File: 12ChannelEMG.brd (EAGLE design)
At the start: 65.9 x 15.4 mm, 24 parts

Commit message: Duplicated first channel to make second channel
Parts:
- added C10: 3.3uF, resistor:C1206K
- added C11, C12: 0.22uF, rcl:C0603K
- added C13, C14, C8, C9: 0.1uF, resistor:C1206K
- added D2: BAT54, diode:SOT23
- added R11: 50k, rcl:R0805
- added R12, R20: 100, resistor:R0603
- added R13: 10k, rcl:R0603
- added R14: 200, rcl:R0603
- added R15, R16: 82k, resistor:R0603
- added R17: 300, resistor:R0603
- added R18: 100k, resistor:R0603
- added R19: 56k, resistor:R0603
- added U$4: INA101KU, 12-ChannelEMG:SOIC167.5MM
- added U$5: LMC6492, 12-ChannelEMG:SOIC14
- added U$6: PV36504, 12-ChannelEMG:PV36W
- added VIN+1, VIN-1: 1.5MMJACK, 12-ChannelEMG:1.5MMTOUCHPROOFJACK
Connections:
- new net N$13: R11.2, U$4.12, U$4.13
- new net N$20: U$4.3, VIN-1.1
- new net N$21: R12.2, U$5.2, U$6.1
- new net N$22: R12.1, U$4.1
- new net N$23: C10.1, U$5.1, U$6.2
- new net N$24: C10.2, R13.2, U$5.5
- new net N$25: R14.1, U$5.6, U$5.7
- new net N$26: R14.2, R20.1, U$5.9
- new net N$27: D2.1, U$5.8
- new net N$28: C13.1, R16.1, U$5.12
- new net N$29: D2.3, R15.1, R17.1, R20.2
- new net N$30: C14.2, R19.2, U$5.14
- new net N$31: R18.1, R19.1, U$5.13
- new net N$32: C14.1, R15.2, R16.2
- new net N$33: R11.1, U$4.4, U$4.5
- new net N$34: U$4.14, VIN+1.1
- net GND: now also C11.2, C12.2, C13.2, C8.2, C9.2, R13.1, R17.2, R18.2, U$5.10, U$5.3
- net VCC+: now also C11.1, C8.1, U$4.2, U$5.4
- net VCC-: now also C12.1, C9.1, U$4.15, U$5.11
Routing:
- net VCC-: track 36.8 -> 86.4 mm
- net VCC+: track 28.1 -> 71.1 mm, vias 2 -> 5
- net N$21: track 0.00 -> 18.0 mm, vias 0 -> 1
- net N$34: track 0.00 -> 15.1 mm, vias 0 -> 1
- net N$29: track 0.00 -> 13.4 mm, vias 0 -> 1
- net N$23: track 0.00 -> 10.1 mm
- net N$24: track 0.00 -> 9.66 mm
- net N$32: track 0.00 -> 8.14 mm
- net N$26: track 0.00 -> 7.74 mm
- net N$20: track 0.00 -> 7.35 mm
- net N$30: track 0.00 -> 5.88 mm, vias 0 -> 1
- net N$28: track 0.00 -> 5.28 mm, vias 0 -> 1
- net N$13: track 0.00 -> 4.66 mm, vias 0 -> 1
- net N$33: track 0.00 -> 4.66 mm, vias 0 -> 1
- net N$31: track 0.00 -> 4.54 mm
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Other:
- board size 65.9 x 15.4 mm -> 65.9 x 269.4 mm

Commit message: Three Channels
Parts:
- added C15, C16, C20, C21: 0.1uF, resistor:C1206K
- added C17: 3.3uF, resistor:C1206K
- added C18, C19: 0.22uF, rcl:C0603K
- added D3: BAT54, diode:SOT23
- added R21: 50k, rcl:R0805
- added R22, R30: 100, resistor:R0603
- added R23: 10k, rcl:R0603
- added R24: 200, rcl:R0603
- added R25, R26: 82k, resistor:R0603
- added R27: 300, resistor:R0603
- added R28: 100k, resistor:R0603
- added R29: 56k, resistor:R0603
- added U$7: INA101KU, 12-ChannelEMG:SOIC167.5MM
- added U$8: LMC6492, 12-ChannelEMG:SOIC14
- added U$9: PV36504, 12-ChannelEMG:PV36W
- added VIN+2, VIN-2: 1.5MMJACK, 12-ChannelEMG:1.5MMTOUCHPROOFJACK
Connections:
- new net N$35: R21.2, U$7.12, U$7.13
- new net N$36: U$7.3, VIN-2.1
- new net N$37: R22.2, U$8.2, U$9.1
- new net N$38: R22.1, U$7.1
- new net N$39: C17.1, U$8.1, U$9.2
- new net N$40: C17.2, R23.2, U$8.5
- new net N$41: R24.1, U$8.6, U$8.7
- new net N$42: R24.2, R30.1, U$8.9
- new net N$43: D3.1, U$8.8
- new net N$44: C20.1, R26.1, U$8.12
- new net N$45: D3.3, R25.1, R27.1, R30.2
- new net N$46: C21.2, R29.2, U$8.14
- new net N$47: R28.1, R29.1, U$8.13
- new net N$48: C21.1, R25.2, R26.2
- new net N$49: R21.1, U$7.4, U$7.5
- new net N$50: U$7.14, VIN+2.1
- net GND: now also C15.2, C16.2, C18.2, C19.2, C20.2, R23.1, R27.2, R28.2, U$8.10, U$8.3
- net VCC+: now also C15.1, C18.1, U$7.2, U$8.4
- net VCC-: now also C16.1, C19.1, U$7.15, U$8.11
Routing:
- net VCC-: track 86.4 -> 136.4 mm
- net VCC+: track 71.1 -> 114.1 mm, vias 5 -> 8
- net N$37: track 0.00 -> 18.0 mm, vias 0 -> 1
- net N$50: track 0.00 -> 15.1 mm, vias 0 -> 1
- net N$45: track 0.00 -> 13.4 mm, vias 0 -> 1
- net N$39: track 0.00 -> 10.1 mm
- net N$40: track 0.00 -> 9.66 mm
- net N$48: track 0.00 -> 8.14 mm
- net N$42: track 0.00 -> 7.74 mm
- net N$36: track 0.00 -> 7.35 mm
- net N$46: track 0.00 -> 5.88 mm, vias 0 -> 1
- net N$44: track 0.00 -> 5.28 mm, vias 0 -> 1
- net N$35: track 0.00 -> 4.66 mm, vias 0 -> 1
- net N$49: track 0.00 -> 4.66 mm, vias 0 -> 1
- net N$47: track 0.00 -> 4.54 mm
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
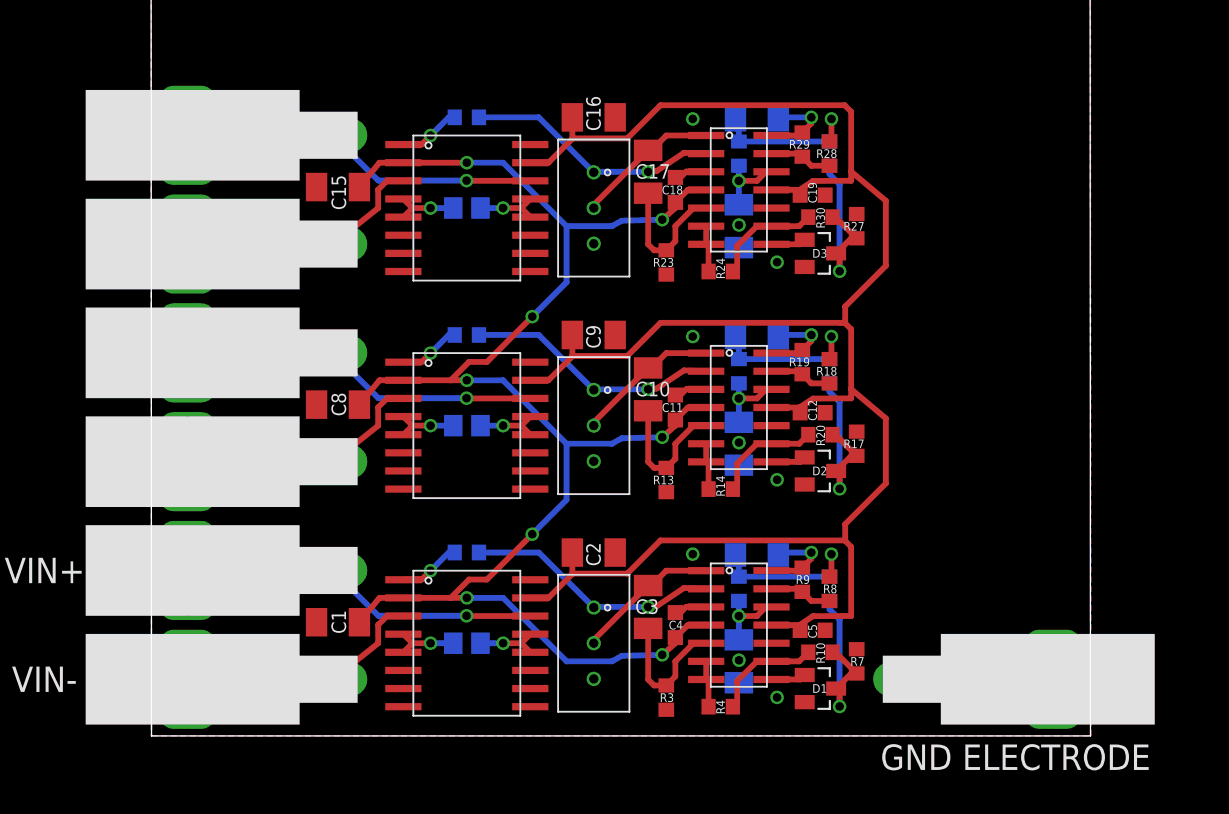
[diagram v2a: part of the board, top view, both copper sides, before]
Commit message: Removed old connectors
Added ground jumper for ground electrode
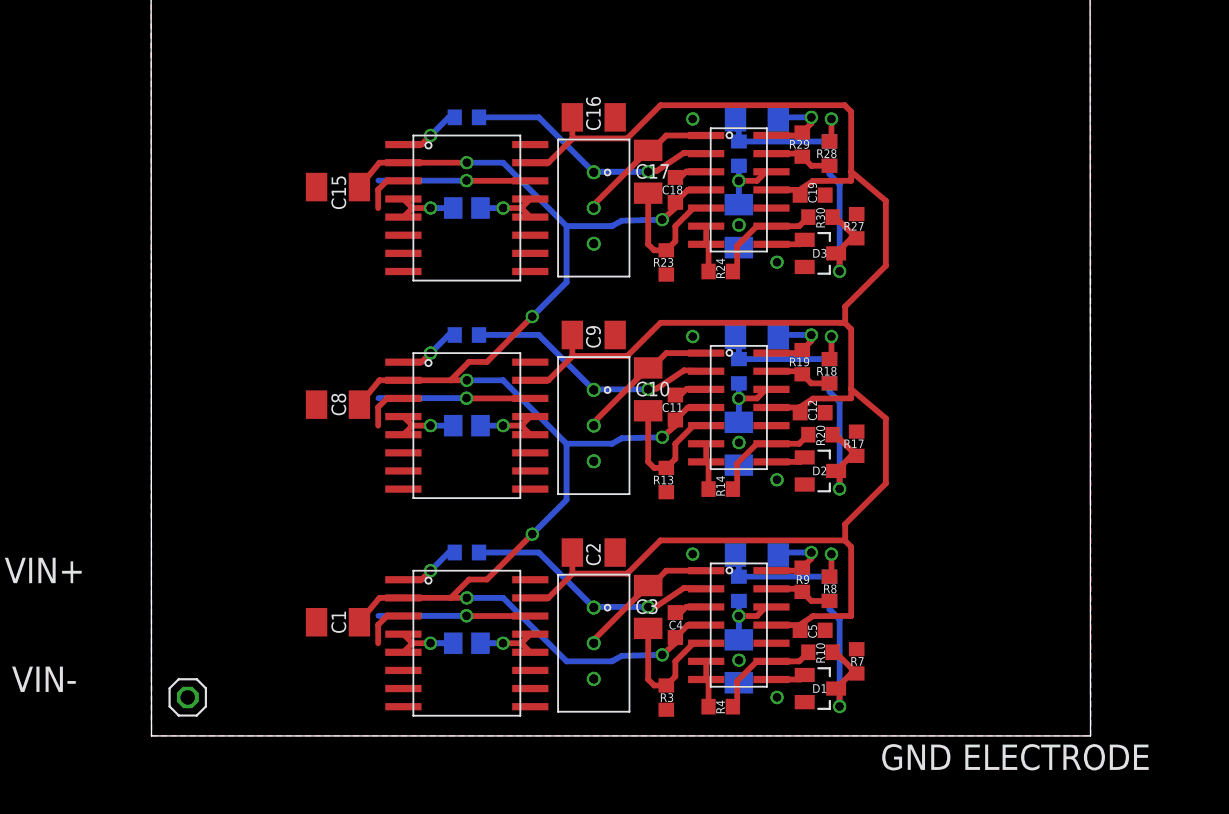
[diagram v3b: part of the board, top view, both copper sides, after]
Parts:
- removed VIN+, VIN+1, VIN+2, VIN-, VIN-1, VIN-2: 1.5MMJACK, 12-ChannelEMG:1.5MMTOUCHPROOFJACK
- GND: value 1.5MMJACK -> GND; device 12-ChannelEMG:1.5MMTOUCHPROOFJACK -> pinhead:1X01
- moved GND 55.5 mm to (2.54, 2.54), turned to 0 degrees
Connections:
- net N$20: no longer VIN-1.1
- net N$34: no longer VIN+1.1
- net N$36: no longer VIN-2.1
- net N$50: no longer VIN+2.1
- net N$6: no longer VIN-.1
- net N$7: no longer VIN+.1
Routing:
- net N$7: track 15.1 -> 10.6 mm
- net N$34: track 15.1 -> 10.6 mm
- net N$50: track 15.1 -> 10.6 mm
- net N$36: track 7.35 -> 3.31 mm
- net N$20: track 7.35 -> 3.31 mm
- net N$6: track 7.35 -> 3.31 mm
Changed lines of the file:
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@@
 <setting verticaltext="up"/>
 </settings>
-<grid distance="50" unitdist="mil" unit="mil" style="lines" multiple="1" display="yes" altdistance="5" altunitdist="mil" altunit="mil"/>
+<grid distance="5" unitdist="mil" unit="mil" style="lines" multiple="1" display="yes" altdistance="5" altunitdist="mil" altunit="mil"/>
 <layers>
 <layer number="1" name="Top" color="4" fill="1" visible="yes" active="yes"/>
@@
 <attribute name="NAME" x="47.168915625" y="4.90091875" size="0.6096" layer="25" rot="R90"/>
 </element>
-<element name="VIN+" library="12-ChannelEMG" package="1.5MMTOUCHPROOFJACK" value="1.5MMJACK" x="7.62" y="11.43"/>
-<element name="VIN-" library="12-ChannelEMG" package="1.5MMTOUCHPROOFJACK" value="1.5MMJACK" x="7.62" y="3.81"/>
-<element name="GND" library="12-ChannelEMG" package="1.5MMTOUCHPROOFJACK" value="1.5MMJACK" x="58.039" y="3.81" rot="R180"/>
 <element name="U$4" library="12-ChannelEMG" package="SOIC167.5MM" value="INA101KU" x="22.0871375" y="21.574346875"/>
 <element name="R11" library="rcl" package="R0805" value="50k" x="22.0871375" y="21.574346875" smashed="yes" rot="MR180">
@@
 <attribute name="NAME" x="47.168915625" y="20.14091875" size="0.6096" layer="25" rot="R90"/>
 </element>
-<element name="VIN+1" library="12-ChannelEMG" package="1.5MMTOUCHPROOFJACK" value="1.5MMJACK" x="7.62" y="26.67"/>
-<element name="VIN-1" library="12-ChannelEMG" package="1.5MMTOUCHPROOFJACK" value="1.5MMJACK" x="7.62" y="19.05"/>
 <element name="U$7" library="12-ChannelEMG" package="SOIC167.5MM" value="INA101KU" x="22.0871375" y="36.814346875"/>
 <element name="R21" library="rcl" package="R0805" value="50k" x="22.0871375" y="36.814346875" smashed="yes" rot="MR180">
@@
 <attribute name="NAME" x="47.168915625" y="35.38091875" size="0.6096" layer="25" rot="R90"/>
 </element>
-<element name="VIN+2" library="12-ChannelEMG" package="1.5MMTOUCHPROOFJACK" value="1.5MMJACK" x="7.62" y="41.91"/>
-<element name="VIN-2" library="12-ChannelEMG" package="1.5MMTOUCHPROOFJACK" value="1.5MMJACK" x="7.62" y="34.29"/>
+<element name="GND" library="pinhead" package="1X01" value="GND" x="2.54" y="2.54" smashed="yes">
+<attribute name="VALUE" x="4.064" y="1.143" size="1.27" layer="27"/>
+</element>
 </elements>
 <signals>
@@
 <wire x1="37.465" y1="8.89" x2="38.835484375" y2="8.89" width="0.4064" layer="1"/>
 <wire x1="38.835484375" y1="8.89" x2="38.8511375" y2="8.874346875" width="0.4064" layer="1"/>
-<contactref element="GND" pad="1"/>
 <contactref element="C9" pad="2"/>
 <contactref element="C8" pad="2"/>
@@
 <wire x1="37.465" y1="39.37" x2="38.835484375" y2="39.37" width="0.4064" layer="1"/>
 <wire x1="38.835484375" y1="39.37" x2="38.8511375" y2="39.354346875" width="0.4064" layer="1"/>
+<contactref element="GND" pad="1"/>
 </signal>
 <signal name="N$6">
 <contactref element="U$1" pad="3"/>
-<contactref element="VIN-" pad="1"/>
 <wire x1="17.6421375" y1="8.239346875" x2="16.494346875" y2="8.239346875" width="0.4064" layer="1"/>
 <wire x1="16.494346875" y1="8.239346875" x2="15.875" y2="7.62" width="0.4064" layer="1"/>
 <wire x1="15.875" y1="7.62" x2="15.875" y2="6.33" width="0.4064" layer="1"/>
-<wire x1="15.875" y1="6.33" x2="12.72" y2="3.81" width="0.4064" layer="1"/>
 </signal>
 <signal name="N$5">
@@
 <signal name="N$7">
 <contactref element="U$1" pad="14"/>
-<contactref element="VIN+" pad="1"/>
 <wire x1="26.5321375" y1="8.239346875" x2="22.240653125" y2="8.239346875" width="0.4064" layer="1"/>
 <wire x1="22.240653125" y1="8.239346875" x2="22.06625" y2="8.255" width="0.4064" layer="1"/>
 <via x="22.06625" y="8.255" extent="1-16" drill="0.6"/>
 <wire x1="22.06625" y1="8.255" x2="15.895" y2="8.255" width="0.4064" layer="16"/>
-<wire x1="15.895" y1="8.255" x2="12.72" y2="11.43" width="0.4064" layer="16"/>
 </signal>
 <signal name="N$13">
@@
 <signal name="N$20">
 <contactref element="U$4" pad="3"/>
-<contactref element="VIN-1" pad="1"/>
 <wire x1="17.6421375" y1="23.479346875" x2="16.494346875" y2="23.479346875" width="0.4064" layer="1"/>
 <wire x1="16.494346875" y1="23.479346875" x2="15.875" y2="22.86" width="0.4064" layer="1"/>
 <wire x1="15.875" y1="22.86" x2="15.875" y2="21.57" width="0.4064" layer="1"/>
-<wire x1="15.875" y1="21.57" x2="12.72" y2="19.05" width="0.4064" layer="1"/>
 </signal>
 <signal name="N$21">
@@
 <signal name="N$34">
 <contactref element="U$4" pad="14"/>
-<contactref element="VIN+1" pad="1"/>
 <wire x1="26.5321375" y1="23.479346875" x2="22.240653125" y2="23.479346875" width="0.4064" layer="1"/>
 <wire x1="22.240653125" y1="23.479346875" x2="22.06625" y2="23.495" width="0.4064" layer="1"/>
 <via x="22.06625" y="23.495" extent="1-16" drill="0.6"/>
 <wire x1="22.06625" y1="23.495" x2="15.895" y2="23.495" width="0.4064" layer="16"/>
-<wire x1="15.895" y1="23.495" x2="12.72" y2="26.67" width="0.4064" layer="16"/>
 </signal>
 <signal name="N$35">
@@
 <signal name="N$36">
 <contactref element="U$7" pad="3"/>
-<contactref element="VIN-2" pad="1"/>
 <wire x1="17.6421375" y1="38.719346875" x2="16.494346875" y2="38.719346875" width="0.4064" layer="1"/>
 <wire x1="16.494346875" y1="38.719346875" x2="15.875" y2="38.1" width="0.4064" layer="1"/>
 <wire x1="15.875" y1="38.1" x2="15.875" y2="36.81" width="0.4064" layer="1"/>
-<wire x1="15.875" y1="36.81" x2="12.72" y2="34.29" width="0.4064" layer="1"/>
 </signal>
 <signal name="N$37">
@@
 <signal name="N$50">
 <contactref element="U$7" pad="14"/>
-<contactref element="VIN+2" pad="1"/>
 <wire x1="26.5321375" y1="38.719346875" x2="22.240653125" y2="38.719346875" width="0.4064" layer="1"/>
 <wire x1="22.240653125" y1="38.719346875" x2="22.06625" y2="38.735" width="0.4064" layer="1"/>
 <via x="22.06625" y="38.735" extent="1-16" drill="0.6"/>
 <wire x1="22.06625" y1="38.735" x2="15.895" y2="38.735" width="0.4064" layer="16"/>
-<wire x1="15.895" y1="38.735" x2="12.72" y2="41.91" width="0.4064" layer="16"/>
 </signal>
 </signals>
-<errors>
-</errors>
 </board>
 </drawing>

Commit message: Two channels, problems fixed
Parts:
- removed C15, C16, C20, C21: 0.1uF, resistor:C1206K
- removed C17: 3.3uF, resistor:C1206K
- removed C18, C19: 0.22uF, rcl:C0603K
- removed D3: BAT54, diode:SOT23
- removed R21: 50k, rcl:R0805
- removed R22, R30: 100, resistor:R0603
- removed R23: 10k, rcl:R0603
- removed R24: 200, rcl:R0603
- removed R25, R26: 82k, resistor:R0603
- removed R27: 300, resistor:R0603
- removed R28: 100k, resistor:R0603
- removed R29: 56k, resistor:R0603
- removed U$8: LMC6492, 12-ChannelEMG:SOIC14
- removed U$9: PV36504, 12-ChannelEMG:PV36W
- added U$10: 2PIN, 12-ChannelEMG:2PIN
- U$7: value INA101KU -> 2PIN; device 12-ChannelEMG:SOIC167.5MM -> 12-ChannelEMG:2PIN
- moved U$7 23.0 mm to (4.93, 21.5)
- moved R13 5.83 mm to (30.3, 16.7)
- moved C10 5.83 mm to (29.0, 23.1)
- moved C11 5.83 mm to (31.0, 21.8)
- moved C12 5.83 mm to (40.6, 21.5)
- moved C13 5.83 mm to (35.4, 19.3)
- moved C9 5.83 mm to (25.2, 26.9)
- moved D2 5.83 mm to (41.1, 17.4)
- moved R11 5.83 mm to (16.3, 20.6)
- moved R12 5.83 mm to (16.3, 26.9)
- moved R14 5.83 mm to (34.1, 16.1)
- moved R15 5.83 mm to (41.7, 24.4)
- moved R16 5.83 mm to (35.4, 24.4)
- moved R18 5.83 mm to (41.7, 24.4)
- moved R19 5.83 mm to (39.8, 25.0)
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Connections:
- removed net N$35: R21.2, U$7.12, U$7.13
- removed net N$36: U$7.3
- removed net N$37: R22.2, U$8.2, U$9.1
- removed net N$38: R22.1, U$7.1
- removed net N$39: C17.1, U$8.1, U$9.2
- removed net N$40: C17.2, R23.2, U$8.5
- removed net N$41: R24.1, U$8.6, U$8.7
- removed net N$42: R24.2, R30.1, U$8.9
- removed net N$43: D3.1, U$8.8
- removed net N$44: C20.1, R26.1, U$8.12
- removed net N$45: D3.3, R25.1, R27.1, R30.2
- removed net N$46: C21.2, R29.2, U$8.14
- removed net N$47: R28.1, R29.1, U$8.13
- removed net N$48: C21.1, R25.2, R26.2
- removed net N$49: R21.1, U$7.4, U$7.5
- removed net N$50: U$7.14
- net GND: no longer C15.2, C16.2, C18.2, C19.2, C20.2, R23.1, R27.2, R28.2, U$8.10, U$8.3
- net N$20: now also U$7.2
- net N$34: now also U$7.1
- net N$6: now also U$10.2
- net N$7: now also U$10.1
- net VCC+: no longer C15.1, C18.1, U$7.2, U$8.4
- net VCC-: no longer C16.1, C19.1, U$7.15, U$8.11
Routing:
- net VCC-: track 136.4 -> 86.7 mm
- net VCC+: track 114.1 -> 74.1 mm, vias 8 -> 5
- net N$37: track 18.0 -> 0.00 mm, vias 1 -> 0
- net N$45: track 13.4 -> 0.00 mm, vias 1 -> 0
- net N$50: track 10.6 -> 0.00 mm, vias 1 -> 0
- net N$39: track 10.1 -> 0.00 mm
- net N$40: track 9.66 -> 0.00 mm
- net N$48: track 8.14 -> 0.00 mm
- net N$42: track 7.74 -> 0.00 mm
- net N$46: track 5.88 -> 0.00 mm, vias 1 -> 0
- net N$44: track 5.28 -> 0.00 mm, vias 1 -> 0
- net N$7: track 10.6 -> 15.9 mm
- net N$34: track 10.6 -> 15.9 mm
- net N$20: track 3.31 -> 8.31 mm
- net N$6: track 3.31 -> 8.31 mm
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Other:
- board size 65.9 x 269.4 mm -> 47.4 x 269.2 mm
- board text removed: "GND ELECTRODE"
- board text removed: "VIN+"
- board text removed: "VIN-"

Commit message: Channel 4
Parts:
- added C15, C16, C20, C21, C22, C23, C27, C28: 0.1uF, resistor:C1206K
- added C17, C24: 3.3uF, resistor:C1206K
- added C18, C19, C25, C26: 0.22uF, rcl:C0603K
- added D3, D4: BAT54, diode:SOT23
- added R21, R31: 50k, rcl:R0805
- added R22, R30, R32, R40: 100, resistor:R0603
- added R23, R33: 10k, rcl:R0603
- added R24, R34: 200, rcl:R0603
- added R25, R26, R35, R36: 82k, resistor:R0603
- added R27, R37: 300, resistor:R0603
- added R28, R38: 100k, resistor:R0603
- added R29, R39: 56k, resistor:R0603
- added U$11, U$15: PV36504, 12-ChannelEMG:PV36W
- added U$12, U$16: 2PIN, 12-ChannelEMG:2PIN
- added U$13, U$8: INA101KU, 12-ChannelEMG:SOIC167.5MM
- added U$14, U$9: LMC6492, 12-ChannelEMG:SOIC14
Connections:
- new net N$35: R21.2, U$8.12, U$8.13
- new net N$36: U$12.2, U$8.3
- new net N$37: R22.2, U$11.1, U$9.2
- new net N$38: R22.1, U$8.1
- new net N$39: C17.1, U$11.2, U$9.1
- new net N$40: C17.2, R23.2, U$9.5
- new net N$41: R24.1, U$9.6, U$9.7
- new net N$42: R24.2, R30.1, U$9.9
- new net N$43: D3.1, U$9.8
- new net N$44: C20.1, R26.1, U$9.12
- new net N$45: D3.3, R25.1, R27.1, R30.2
- new net N$46: C21.2, R29.2, U$9.14
- new net N$47: R28.1, R29.1, U$9.13
- new net N$48: C21.1, R25.2, R26.2
- new net N$49: R21.1, U$8.4, U$8.5
- new net N$50: U$12.1, U$8.14
- new net N$51: R31.2, U$13.12, U$13.13
- new net N$52: U$13.3, U$16.2
- new net N$53: R32.2, U$14.2, U$15.1
- new net N$54: R32.1, U$13.1
- new net N$55: C24.1, U$14.1, U$15.2
- new net N$56: C24.2, R33.2, U$14.5
- new net N$57: R34.1, U$14.6, U$14.7
- new net N$58: R34.2, R40.1, U$14.9
- new net N$59: D4.1, U$14.8
- new net N$60: C27.1, R36.1, U$14.12
- new net N$61: D4.3, R35.1, R37.1, R40.2
- new net N$62: C28.2, R39.2, U$14.14
- new net N$63: R38.1, R39.1, U$14.13
- new net N$64: C28.1, R35.2, R36.2
- new net N$65: R31.1, U$13.4, U$13.5
- new net N$66: U$13.14, U$16.1
- net GND: now also C15.2, C16.2, C18.2, C19.2, C20.2, C22.2, C23.2, C25.2, C26.2, C27.2, R23.1, R27.2, R28.2, R33.1, R37.2, R38.2, U$14.10, U$14.3, U$9.10, U$9.3
- net VCC+: now also C15.1, C18.1, C22.1, C25.1, U$13.2, U$14.4, U$8.2, U$9.4
- net VCC-: now also C16.1, C19.1, C23.1, C26.1, U$13.15, U$14.11, U$8.15, U$9.11
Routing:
- net VCC-: track 86.7 -> 182.7 mm
- net VCC+: track 74.1 -> 158.7 mm, vias 5 -> 11
- net N$37: track 0.00 -> 18.0 mm, vias 0 -> 1
- net N$53: track 0.00 -> 18.0 mm, vias 0 -> 1
- net N$66: track 0.00 -> 15.9 mm, vias 0 -> 1
- net N$50: track 0.00 -> 15.9 mm, vias 0 -> 1
- net N$45: track 0.00 -> 13.4 mm, vias 0 -> 1
- net N$61: track 0.00 -> 13.4 mm, vias 0 -> 1
- net N$39: track 0.00 -> 10.1 mm
- net N$55: track 0.00 -> 10.1 mm
- net N$56: track 0.00 -> 9.66 mm
- net N$40: track 0.00 -> 9.66 mm
- net N$36: track 0.00 -> 8.31 mm
- net N$52: track 0.00 -> 8.31 mm
- net N$64: track 0.00 -> 8.14 mm
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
